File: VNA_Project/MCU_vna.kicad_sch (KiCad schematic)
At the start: 34 parts, among them SW201 SW_Push, U402 ESP32-S3, U403 MX25L6433FM2I-08G, U404 ESP-PSRAM32, Y201 Crystal_GND24

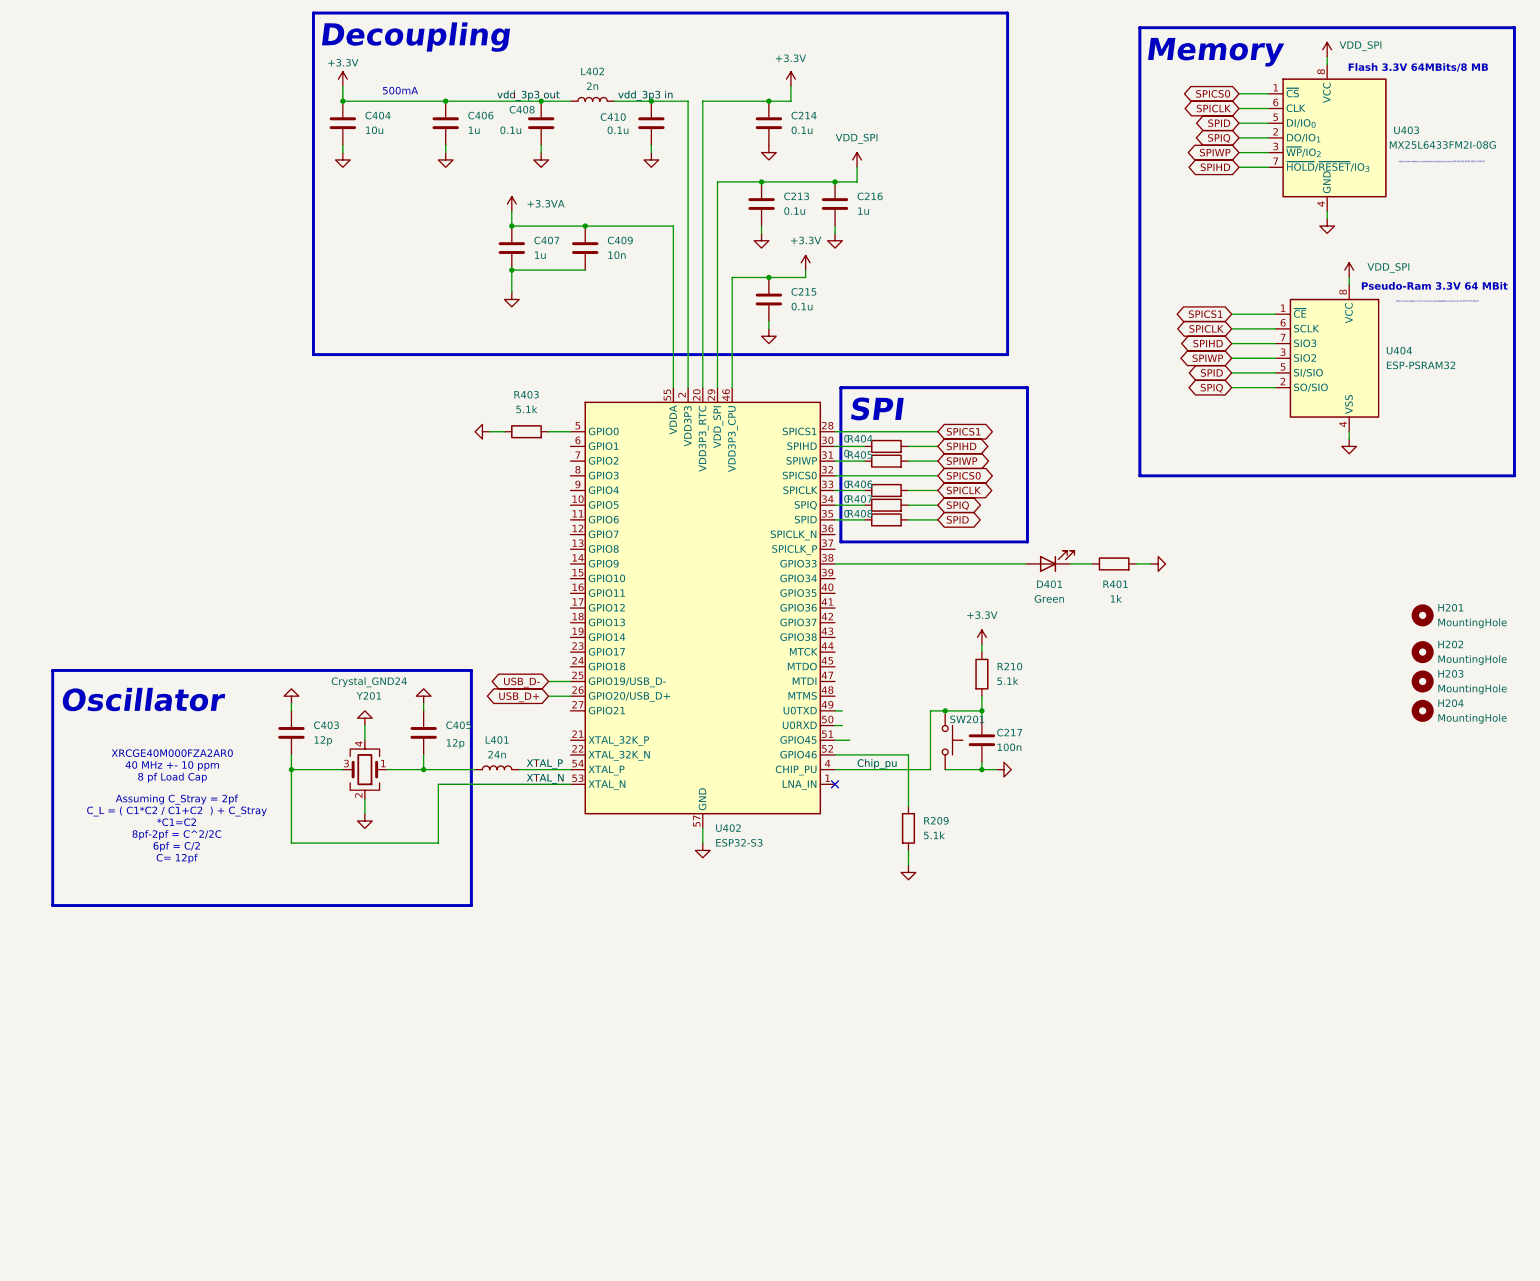
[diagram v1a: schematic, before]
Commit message: Changing from a ESP32 S3 to STM32 H7 high performance MCU for USB HS and ETH capabilities
Changing from a ESP32 S3 to STM32 H7 high performance MCU for USB HS and ETH capabilities
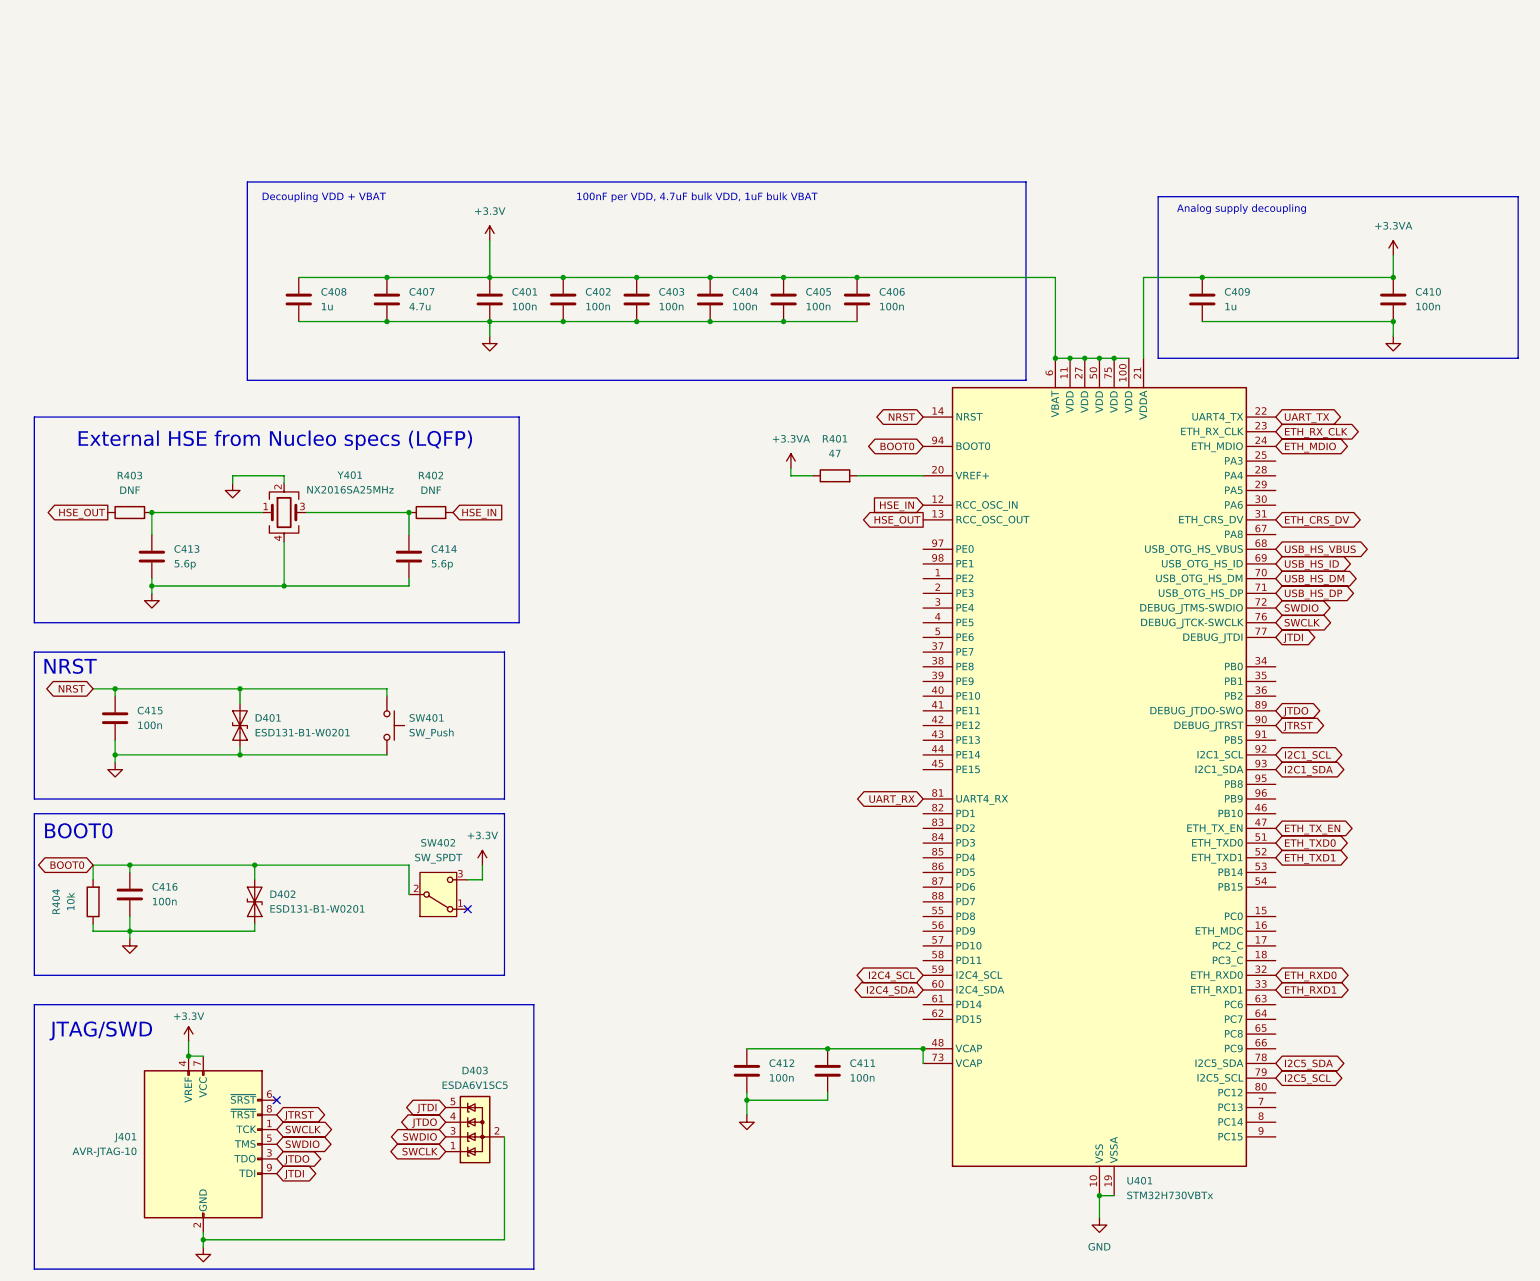
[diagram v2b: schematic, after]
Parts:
- removed C213, C214, C215: 0.1u, Capacitor_SMD:C_0402_1005Metric_Pad0.74x0.62mm_HandSolder, symbol Device:C
- removed C216: 1u, Capacitor_SMD:C_0603_1608Metric_Pad1.08x0.95mm_HandSolder, symbol Device:C
- removed C217: 100n, Capacitor_SMD:C_0402_1005Metric_Pad0.74x0.62mm_HandSolder, symbol Device:C
- removed D401: Green, symbol Device:LED
- removed H201, H202, H203, H204: MountingHole, MountingHole:MountingHole_3.2mm_M3, symbol Mechanical:MountingHole
- removed L401: 24n, Inductor_SMD:L_0402_1005Metric_Pad0.77x0.64mm_HandSolder, symbol Device:L
- removed L402: 2n, Inductor_SMD:L_0402_1005Metric_Pad0.77x0.64mm_HandSolder, symbol Device:L
- removed R209, R210: 5.1k, Resistor_SMD:R_0402_1005Metric_Pad0.72x0.64mm_HandSolder, symbol Device:R
- removed R405, R406, R407, R408: 0, Resistor_SMD:R_0402_1005Metric_Pad0.72x0.64mm_HandSolder, symbol Device:R
- removed SW201: SW_Push, Button_Switch_THT:SW_PUSH_6mm_H4.3mm, symbol Switch:SW_Push
- removed U402: ESP32-S3, Package_DFN_QFN:QFN-56-1EP_7x7mm_P0.4mm_EP4x4mm, symbol MCU_Espressif:ESP32-S3
- removed U403: MX25L6433FM2I-08G, Package_SO:SOIC-8_5.3x5.3mm_P1.27mm, symbol Memory_Flash:W25Q32JVSS
- removed U404: ESP-PSRAM32, Package_SO:SOIC-8_3.9x4.9mm_P1.27mm, symbol Memory_RAM:ESP-PSRAM32
- removed Y201: Crystal_GND24, Crystal:Crystal_SMD_SeikoEpson_FA128-4Pin_2.0x1.6mm, symbol Device:Crystal_GND24
- added C401, C402, C411, C412, C415, C416: 100n, symbol Device:C
- added C413, C414: 5.6p, symbol Device:C
- added D401, D402: ESD131-B1-W0201, Diode_SMD:Infineon_SG-WLL-2-3_0.58x0.28_P0.36mm, symbol Diode:ESD131-B1-W0201
- added D403: ESDA6V1SC5, Package_TO_SOT_SMD:SOT-23-5, symbol Power_Protection:ESDA6V1SC5
- added J401: AVR-JTAG-10, symbol Connector:AVR-JTAG-10
- added R402: DNF, symbol Device:R
- added SW401: SW_Push, symbol Switch:SW_Push
- added SW402: SW_SPDT, symbol Switch:SW_SPDT
- added U401: STM32H730VBTx, Package_QFP:LQFP-100_14x14mm_P0.5mm, symbol MCU_ST_STM32H7:STM32H730VBTx
- added Y401: NX2016SA25MHz, symbol Device:Crystal_GND24
- C403, C405: value 12p -> 100n; footprint Capacitor_SMD:C_0402_1005Metric_Pad0.74x0.62mm_HandSolder -> (none)
- C404: value 10u -> 100n; footprint Capacitor_SMD:C_0603_1608Metric_Pad1.08x0.95mm_HandSolder -> (none)
- C406: value 1u -> 100n; footprint Capacitor_SMD:C_0603_1608Metric_Pad1.08x0.95mm_HandSolder -> (none)
- C407: value 1u -> 4.7u; footprint Capacitor_SMD:C_0603_1608Metric_Pad1.08x0.95mm_HandSolder -> (none)
- C408: value 0.1u -> 1u; footprint Capacitor_SMD:C_0402_1005Metric_Pad0.74x0.62mm_HandSolder -> (none)
- C409: value 10n -> 1u; footprint Capacitor_SMD:C_0402_1005Metric_Pad0.74x0.62mm_HandSolder -> (none)
- C410: value 0.1u -> 100n; footprint Capacitor_SMD:C_0402_1005Metric_Pad0.74x0.62mm_HandSolder -> (none)
- R401: value 1k -> 47
- R403: value 5.1k -> DNF; footprint Resistor_SMD:R_0402_1005Metric_Pad0.72x0.64mm_HandSolder -> (none)
- R404: value 0 -> 10k; footprint Resistor_SMD:R_0402_1005Metric_Pad0.72x0.64mm_HandSolder -> (none)
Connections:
- net XTAL_N is gone; now on net +3.3V: C403.1
- net vdd_3p3 in is gone; now on net GND: C410.2
- net +3.3V: now also C404.1, C405.1, C406.1, C407.1, C408.1, C401.1, C402.1, J401.4 (VREF), J401.7 (VCC), SW402.3 (C), U401.100 (VDD), U401.11 (VDD), U401.27 (VDD), U401.50 (VDD), U401.6 (VBAT), U401.75 (VDD); no longer C404.2, C406.2, C408.2
- net +3.3VA: now also C410.1, R401.1, U401.21 (VDDA); no longer C407.1
- net GND: now also C404.2, C406.2, C408.2, R404.1, C401.2, C402.2, C411.2, C412.2, C413.2, C414.2, C415.2, C416.2, D401.1 (A1), D402.1 (A1), D403.2 (A), J401.10 (GND), J401.2 (GND), SW401.2, U401.10 (VSS), U401.19 (VSSA), U401.26 (VSS), U401.49 (VSS), U401.74 (VSS), U401.99 (VSS), Y401.2, Y401.4; no longer C404.1, C406.1, C408.1, C410.1, R401.2, R403.1
- net at R403.2: now also C413.1, Y401.1
- net SPIHD renamed BOOT0
- net BOOT0: now also C416.1, D402.2 (A2), SW402.2 (B), U401.94 (BOOT0)
- new net: R401.2, U401.20 (VREF+)
- new net: C411.1, C412.1, U401.48 (VCAP), U401.73 (VCAP)
- new net: C414.1, R402.1, Y401.3
- new net ETH_CRS_DV: U401.31 (PA7)
- new net ETH_MDIO: U401.24 (PA2)
- new net ETH_RXD0: U401.32 (PC4)
- new net ETH_RXD1: U401.33 (PC5)
- new net ETH_RX_CLK: U401.23 (PA1)
- new net ETH_TXD0: U401.51 (PB12)
- new net ETH_TXD1: U401.52 (PB13)
- new net ETH_TX_EN: U401.47 (PB11)
- new net HSE_IN: R402.2, U401.12 (PH0)
- new net HSE_OUT: R403.1, U401.13 (PH1)
- new net I2C1_SCL: U401.92 (PB6)
- new net I2C1_SDA: U401.93 (PB7)
- new net I2C4_SCL: U401.59 (PD12)
- new net I2C4_SDA: U401.60 (PD13)
- new net I2C5_SCL: U401.79 (PC11)
- new net I2C5_SDA: U401.78 (PC10)
- new net JTDI: D403.5 (K), J401.9 (TDI), U401.77 (PA15(JTDI))
- new net JTDO: D403.4 (K), J401.3 (TDO), U401.89 (PB3(JTDO)
- new net JTRST: J401.8 (~{TRST}), U401.90 (PB4(NJTRST))
- new net NRST: C415.1, D401.2 (A2), SW401.1, U401.14 (NRST)
- new net SWCLK: D403.1 (K), J401.1 (TCK), U401.76 (PA14(JTCK)
- new net SWDIO: D403.3 (K), J401.5 (TMS), U401.72 (PA13(JTMS)
- new net UART_RX: U401.81 (PD0)
- new net UART_TX: U401.22 (PA0)
- new net USB_HS_DM: U401.70 (PA11)
- new net USB_HS_DP: U401.71 (PA12)
- new net USB_HS_ID: U401.69 (PA10)
- new net USB_HS_VBUS: U401.68 (PA9)
- no-connect marks 1 -> 2
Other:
- note added: "100nF per VDD, 4.7uF bulk VDD, 1uF bulk VBAT"
- note added: "Analog supply decoupling"
- note added: "BOOT0"
- note added: "Decoupling VDD + VBAT"
- note added: "External HSE from Nucleo specs (LQFP)"
- note added: "JTAG/SWD"
- note added: "NRST"
- note removed: "500mA"
- note removed: "Assuming C_Stray = 2pf C_L = ( C1*C2 / C1+C2 ) + C_Stray *C1=C2 8pf-2pf = C^2/2C 6pf = C/2 C= 12pf"
- note removed: "Decoupling"
- note removed: "Flash 3.3V 64MBits/8 MB"
- note removed: "Memory"
- note removed: "Oscillator"
- note removed: "Pseudo-Ram 3.3V 64 MBit"
- note removed: "SPI"
- note removed: "XRCGE40M000FZA2AR0 40 MHz +- 10 ppm 8 pf Load Cap"
- note removed: "https://www.digikey.com/en/products/detail/adafruit-industries-llc/4677/13148775"
- note removed: "https://www.digikey.com/en/products/detail/macronix/MX25L6433FM2I-08G/7796740"

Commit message: minor changes
minor changes
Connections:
- net USB_HS_DM renamed USB_HS_D-
- net USB_HS_DP renamed USB_HS_D+
- net USB_HS_ID: no longer names the net of U401.69 (PA10)

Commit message: minor changes
minor changes
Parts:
- removed D403: ESDA6V1SC5, Package_TO_SOT_SMD:SOT-23-5, symbol Power_Protection:ESDA6V1SC5
- removed J401: AVR-JTAG-10, symbol Connector:AVR-JTAG-10
- added C18: 100nF, Capacitor_SMD:C_0402_1005Metric, symbol Device:C
- added D403, D404, D405, D406, D407, D408, D409, D410: ESD131-B1-W0201, Diode_SMD:Infineon_SG-WLL-2-3_0.58x0.28_P0.36mm, symbol Diode:ESD131-B1-W0201
- added FB401: FerriteBead, symbol Device:FerriteBead
- added J2: SWD TC2030, Connector:Tag-Connect_TC2030-IDC-FP_2x03_P1.27mm_Vertical, symbol Connector:Conn_ARM_SWD_TagConnect_TC2030
- added J401, J402: Conn_01x04_Pin, symbol Connector:Conn_01x04_Pin
- added J403, J5: Conn_01x04_Pin, Connector_PinSocket_2.00mm:PinSocket_1x04_P2.00mm_Vertical, symbol Connector:Conn_01x04_Pin
- added R405, R406, R8, R9: 1.5K, Resistor_SMD:R_0402_1005Metric, symbol Device:R
- added R5, R6: 220R, Resistor_SMD:R_0402_1005Metric, symbol Device:R
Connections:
- net +3.3V: now also J2.1 (VCC), J401.1 (Pin_1), J402.1 (Pin_1), J403.1 (Pin_1), J5.1 (Pin_1), R405.1, R406.1, R8.1, R9.1
- net +3.3VA: now also FB401.2; no longer C409.1, C410.1, U401.21 (VDDA)
- net GND: now also C18.1, D403.1 (A1), D404.1 (A1), D405.1 (A1), D406.1 (A1), D407.1 (A1), D408.1 (A1), D409.1 (A1), D410.1 (A1), J2.5 (GND), J401.4 (Pin_4), J402.4 (Pin_4), J403.4 (Pin_4), J5.4 (Pin_4)
- net I2C1_SCL: now also D407.2 (A2), J5.2 (Pin_2), R8.2
- net I2C1_SDA: now also D408.2 (A2), J5.3 (Pin_3), R9.2
- net I2C4_SCL: now also D409.2 (A2), J403.2 (Pin_2), R405.2
- net I2C4_SDA: now also D410.2 (A2), J403.3 (Pin_3), R406.2
- net JTDO: now also J2.6 (SWO)
- net NRST: now also C18.2, J2.3 (~{RESET})
- net SWCLK: now also D405.2 (A2), J2.2 (SWDIO), J402.3 (Pin_3)
- net SWDIO: now also D404.2 (A2), J2.4 (SWCLK), J402.2 (Pin_2)
- net UART_RX: now also D406.2 (A2), R6.2
- net UART_TX: now also R5.2
- net vref+: now reaches R401.2, U401.20 (VREF+)
- new net: D403.2 (A2), J401.2 (Pin_2), R5.1
- new net: J401.3 (Pin_3), R6.1
- new net analog decoupling: C409.1, C410.1, FB401.1, U401.21 (VDDA)
- no-connect marks 2 -> 1
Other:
- note added: "2 - I2C4"
- note added: "I2C1"
- note added: "SWD"
- note added: "SWD 2"
- note added: "UART"
- note removed: "JTAG/SWD"
- moved on the sheet: C409, C410

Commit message: minor changes eth
minor changes eth
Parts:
- added D411, D412: ESD131-B1-W0201, Diode_SMD:Infineon_SG-WLL-2-3_0.58x0.28_P0.36mm, symbol Diode:ESD131-B1-W0201
- added J404: Conn_01x04_Pin, Connector_PinSocket_2.00mm:PinSocket_1x04_P2.00mm_Vertical, symbol Connector:Conn_01x04_Pin
- added R407, R408: 1.5K, Resistor_SMD:R_0402_1005Metric, symbol Device:R
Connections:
- net +3.3V: now also J404.1 (Pin_1), R407.1, R408.1
- net GND: now also D411.1 (A1), D412.1 (A1), J404.4 (Pin_4)
- net I2C5_SCL: now also D411.2 (A2), J404.2 (Pin_2), R407.2
- net I2C5_SDA: now also D412.2 (A2), J404.3 (Pin_3), R408.2
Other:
- note added: "3 - I2C5"
- moved on the sheet: C18, J2

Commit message: Eth done
Eth done
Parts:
- removed R403: DNF, symbol Device:R
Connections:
- net HSE_OUT: now also C413.1, Y401.1
- net ETH_MDC: now reaches U401.16 (PC1)
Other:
- note added: "External HSE"
- note removed: "External HSE from Nucleo specs (LQFP)"

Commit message: minor changes
minor changes
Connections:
- net UART_RX: no longer D406.2 (A2)
- net at J401.3 (Pin_3), R6.1: now also D406.2 (A2)
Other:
- moved on the sheet: D406, D407, D408, R5, R6

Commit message: adc
adc
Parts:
- added D2, D3: ESD131-B1-W0201, Diode_SMD:Infineon_SG-WLL-2-3_0.58x0.28_P0.36mm, symbol Diode:ESD131-B1-W0201
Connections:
- net GND: now also D2.1 (A1), D3.1 (A1)
- net SWCLK: now also D3.2 (A2)
- net SWDIO: now also D2.2 (A2)
- net UART_RX: no longer U401.81 (PD0)
- net UART_TX: no longer U401.22 (PA0)
- net D2_A: now reaches U401.1 (PE2)
- net D3_A: now reaches U401.2 (PE3)
- net D4_A: now reaches U401.3 (PE4)
- net D7_A: now reaches U401.37 (PE7)
- net D8_A: now reaches U401.38 (PE8)
- net D9_A: now reaches U401.39 (PE9)
- net D5_A: now reaches U401.4 (PE5)
- net D10_A: now reaches U401.40 (PE10)
- net D11_A: now reaches U401.41 (PE11)
- net D6_A: now reaches U401.5 (PE6)
- net D8_B: now reaches U401.55 (PD8)
- net D9_B: now reaches U401.56 (PD9)
- net D10_B: now reaches U401.57 (PD10)
- net D11_B: now reaches U401.58 (PD11)
- net D1_B: now reaches U401.82 (PD1)
- net D2_B: now reaches U401.83 (PD2)
- net D3_B: now reaches U401.84 (PD3)
- net D4_B: now reaches U401.85 (PD4)
- net D5_B: now reaches U401.86 (PD5)
- net D6_B: now reaches U401.87 (PD6)
- net D7_B: now reaches U401.88 (PD7)
- net D0_A: now reaches U401.97 (PE0)
- net D1_A: now reaches U401.98 (PE1)
- net USB_HS_D+ renamed USB_D+
- net USB_HS_D- renamed USB_D-
- net USB_HS_VBUS renamed USB_VBUS
- new net D0_B: U401.81 (PD0)
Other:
- note added: "ADC DATA A"
- note added: "ADC DATA B"
- moved on the sheet: C18, J2
